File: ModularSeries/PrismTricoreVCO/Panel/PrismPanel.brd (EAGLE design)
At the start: 50.5 x 128.5 mm, 9 parts

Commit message: Pulse output fixed on Knives, schematics and layout updated. Panel added for Portals
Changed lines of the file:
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@@
 <text x="25" y="-1" size="1.778" layer="21" font="vector" ratio="12" align="center">Sine
 Shape</text>
-<text x="25.25" y="-11" size="3.81" layer="1" font="vector" ratio="12" align="center">P R I S M</text>
-<text x="25.25" y="-11" size="3.81" layer="29" font="vector" ratio="12" align="center">P R I S M</text>
+<text x="25.25" y="-11" size="3.81" layer="1" font="vector" ratio="16" align="center">P R I S M</text>
+<text x="25.25" y="-11" size="3.81" layer="29" font="vector" ratio="16" align="center">P R I S M</text>
 <wire x1="26" y1="9" x2="35" y2="9" width="2" layer="29" curve="-90"/>
 <wire x1="35" y1="9" x2="43" y2="9" width="2" layer="29" curve="90"/>

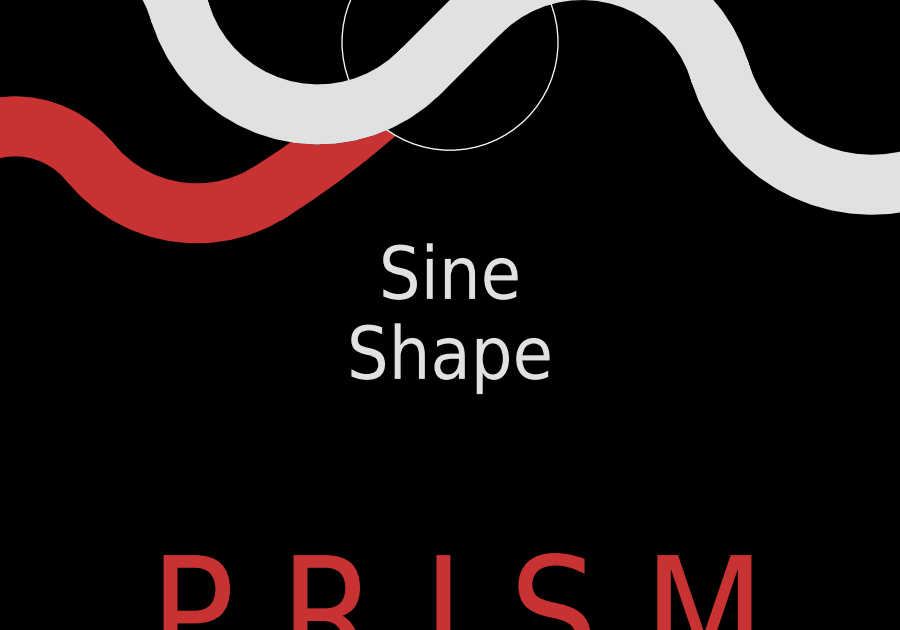
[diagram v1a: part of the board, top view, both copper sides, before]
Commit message: Panel for TimeSeeds added. TLHP core PCB added
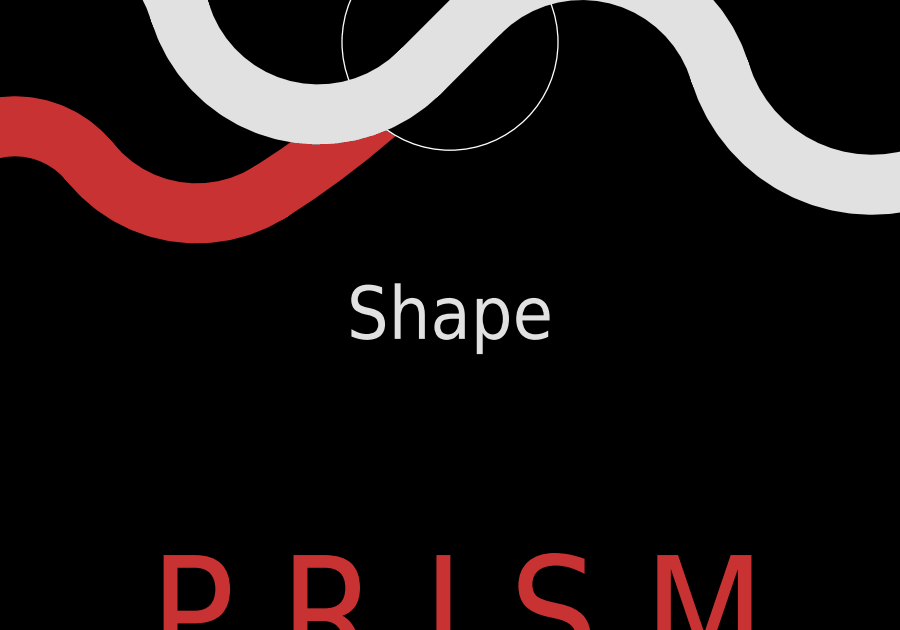
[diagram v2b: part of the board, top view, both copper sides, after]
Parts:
- added E$10: (no value), ElectricNoodleBox:LOGO20X20
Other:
- board text added: "Shape"
- board text removed: "Sine Shape"
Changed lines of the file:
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@@
 <layer number="14" name="Route14" color="22" fill="1" visible="no" active="no"/>
 <layer number="15" name="Route15" color="23" fill="1" visible="no" active="no"/>
-<layer number="16" name="Bottom" color="1" fill="1" visible="no" active="yes"/>
-<layer number="17" name="Pads" color="2" fill="1" visible="no" active="yes"/>
-<layer number="18" name="Vias" color="2" fill="1" visible="no" active="yes"/>
-<layer number="19" name="Unrouted" color="6" fill="1" visible="no" active="yes"/>
+<layer number="16" name="Bottom" color="1" fill="1" visible="yes" active="yes"/>
+<layer number="17" name="Pads" color="2" fill="1" visible="yes" active="yes"/>
+<layer number="18" name="Vias" color="2" fill="1" visible="yes" active="yes"/>
+<layer number="19" name="Unrouted" color="6" fill="1" visible="yes" active="yes"/>
 <layer number="20" name="Dimension" color="24" fill="1" visible="yes" active="yes"/>
 <layer number="21" name="tPlace" color="7" fill="1" visible="yes" active="yes"/>
-<layer number="22" name="bPlace" color="7" fill="1" visible="no" active="yes"/>
-<layer number="23" name="tOrigins" color="15" fill="1" visible="no" active="yes"/>
-<layer number="24" name="bOrigins" color="15" fill="1" visible="no" active="yes"/>
+<layer number="22" name="bPlace" color="7" fill="1" visible="yes" active="yes"/>
+<layer number="23" name="tOrigins" color="15" fill="1" visible="yes" active="yes"/>
+<layer number="24" name="bOrigins" color="15" fill="1" visible="yes" active="yes"/>
 <layer number="25" name="tNames" color="7" fill="1" visible="no" active="yes"/>
 <layer number="26" name="bNames" color="7" fill="1" visible="no" active="yes"/>
@@
 <layer number="47" name="Measures" color="7" fill="1" visible="no" active="yes"/>
 <layer number="48" name="Document" color="7" fill="1" visible="no" active="yes"/>
-<layer number="49" name="Reference" color="7" fill="1" visible="yes" active="yes"/>
+<layer number="49" name="Reference" color="7" fill="1" visible="no" active="yes"/>
 <layer number="50" name="dxf" color="7" fill="1" visible="no" active="no"/>
 <layer number="51" name="tDocu" color="7" fill="1" visible="no" active="yes"/>
@@
 <text x="18" y="35" size="1.778" layer="21" font="vector" ratio="12" align="center">Fine</text>
 <text x="34" y="19" size="1.778" layer="21" font="vector" ratio="12" align="center">FM</text>
-<text x="25" y="-1" size="1.778" layer="21" font="vector" ratio="12" align="center">Sine
-Shape</text>
+<text x="25" y="-1" size="1.778" layer="21" font="vector" ratio="12" align="center">Shape</text>
 <text x="25.25" y="-11" size="3.81" layer="1" font="vector" ratio="16" align="center">P R I S M</text>
 <text x="25.25" y="-11" size="3.81" layer="29" font="vector" ratio="16" align="center">P R I S M</text>
@@
 <element name="E$8" library="ElectricNoodleBox" package="ALPHA9MM_POT_CUTOUT" value="" x="40" y="25" smashed="yes"/>
 <element name="E$9" library="ElectricNoodleBox" package="ALPHA9MM_POT_CUTOUT" value="" x="25" y="8" smashed="yes"/>
+<element name="E$10" library="ElectricNoodleBox" package="LOGO20X20" value="" x="34.5" y="94.5" smashed="yes" rot="MR0"/>
 </elements>
 <signals>
@@
 </drawing>
 <compatibility>
-<note version="6.3" minversion="6.2.2" severity="warning">
-Since Version 6.2.2 text objects can contain more than one line,
-which will not be processed correctly with this version.
-</note>
 <note version="8.3" severity="warning">
 Since Version 8.3, EAGLE supports Fusion synchronisation.
